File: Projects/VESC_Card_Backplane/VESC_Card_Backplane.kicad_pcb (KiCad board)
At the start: 2 copper layers, 40 parts, among them M1 FE1.1S, P1 USB_OTG, P10 AMP17614426-2_EDGE, P11 CONN_01X06, P2 EC90_Flat, P3 AMP17614426-2_EDGE, P4 CONN_01X06, P5 CONN_01X04, P5V1 CONN_01X02, P6 EC90_Flat, P7 AMP17614426-2_EDGE, P8 CONN_01X06, P9 EC90_Flat, U1 LP38693

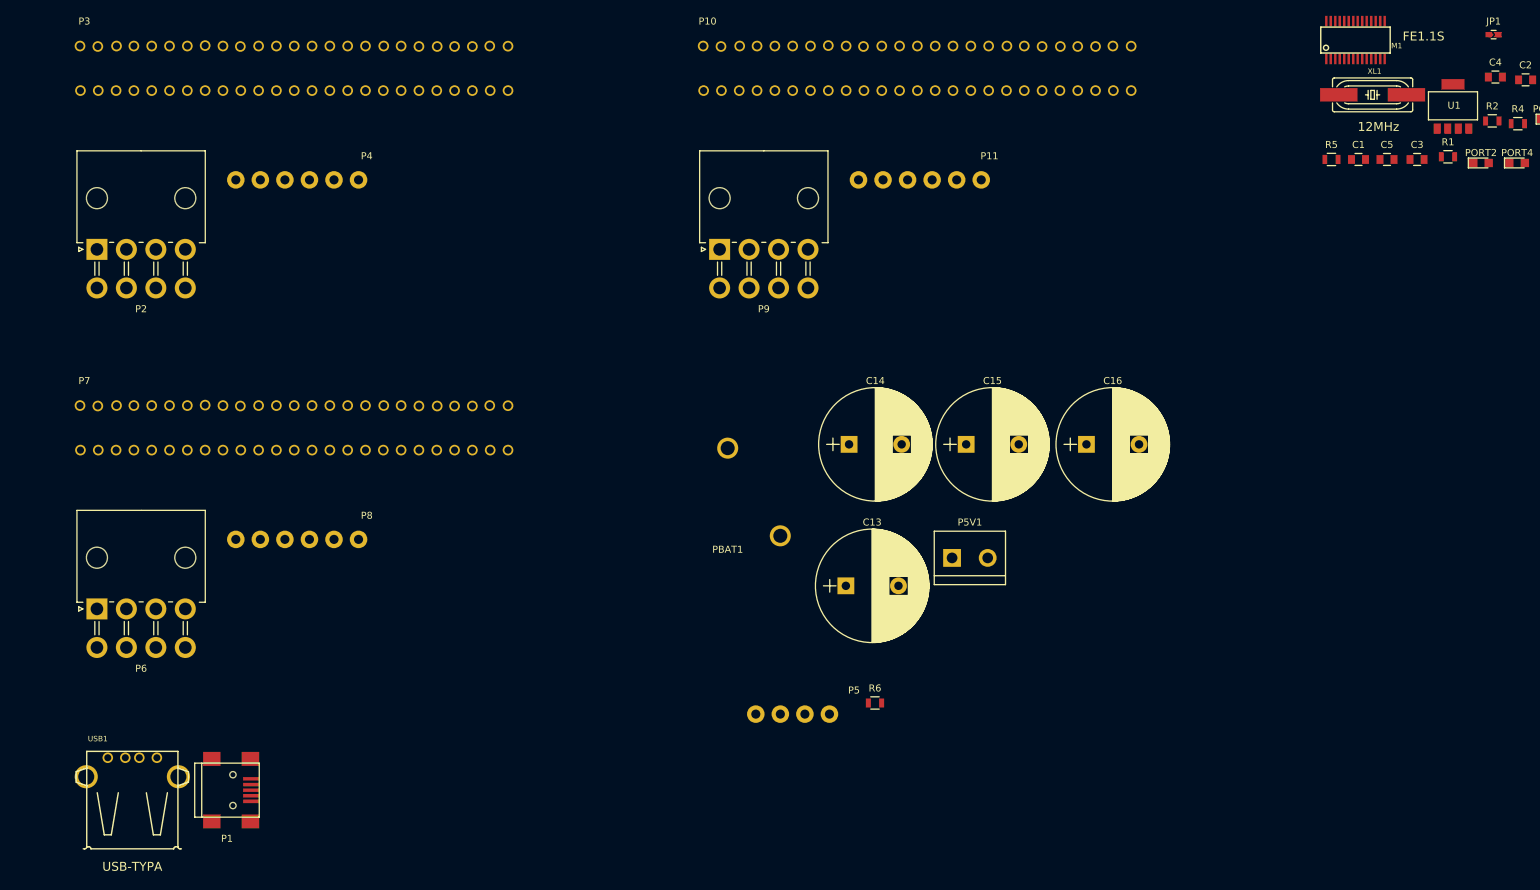
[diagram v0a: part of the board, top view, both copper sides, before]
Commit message: Fixed backplane slot orientation
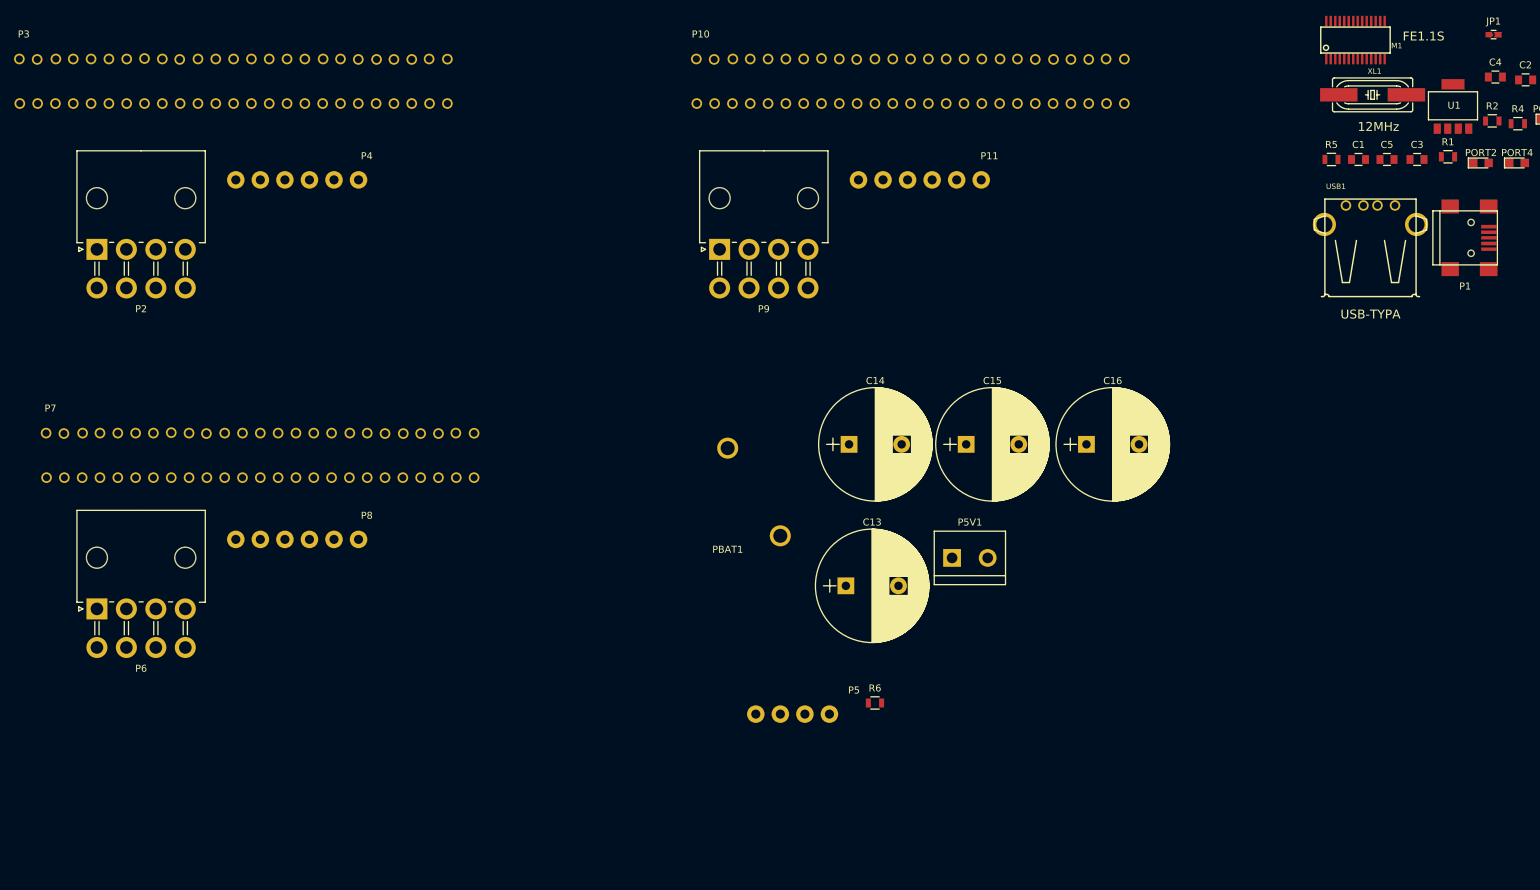
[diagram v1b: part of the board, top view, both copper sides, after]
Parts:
- moved P1 193.3 mm to (241.6, 62.3)
- moved USB1 193.3 mm to (228.1, 63.1)
- moved P3 8.84 mm to (71.1, 50.8)
- moved P7 6.23 mm to (74.9, 104.1)
- moved P10 2.09 mm to (167.6, 50.8)

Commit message: Connected DP's and DM's
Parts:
- ACT1, C1, C2, C3, C4, C5, C6, JP1, PORT1, PORT2, PORT3, PORT4, R1, R2, R3, R4, R5, R6, REXT1, U1: moved to B.Cu
- C14: footprint Capacitors_THT:CP_Radial_D16.0mm_P7.50mm -> Capacitors_ThroughHole:CP_Radial_D8.0mm_P3.80mm
- moved JP1 210.5 mm to (72.9, 153.6), turned to 270 degrees
- moved ACT1 196.0 mm to (82.1, 127.8), turned to 270 degrees
- moved USB1 195.1 mm to (67.6, 173.9)
- moved P1 194.6 mm to (84.2, 176.8), turned to 90 degrees
- moved PORT1 193.0 mm to (82.1, 114.5), turned to 270 degrees
- moved R3 191.4 mm to (91.5, 126.5), turned to 180 degrees
- moved REXT1 189.7 mm to (86.7, 127.9), turned to 180 degrees
- moved XL1 187.1 mm to (83.9, 160.8), turned to 270 degrees
- moved C2 185.4 mm to (84.7, 123.3), turned to 270 degrees
- moved R4 182.7 mm to (81.9, 119.6)
- moved PORT3 182.1 mm to (86.2, 117.2)
- moved M1 181.4 mm to (84.0, 147.1), turned to 180 degrees
- moved C6 177.0 mm to (91.9, 102.9), turned to 90 degrees
- moved PORT4 175.1 mm to (88.6, 121.8), turned to 270 degrees
- moved R2 172.6 mm to (86.7, 113.5)
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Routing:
- net /PGND: track 0.00 -> 167.6 mm
- net +5V: track 0.00 -> 114.8 mm
- net /USB_DP_1: track 0.00 -> 98.2 mm, vias 0 -> 1
- net /USB_DM_1: track 0.00 -> 97.3 mm, vias 0 -> 1
- net /USB_DM_2: track 0.00 -> 66.6 mm
- net /Motor_Controller_A/Y: track 0.00 -> 62.3 mm
- net /USB_DP_2: track 0.00 -> 58.9 mm
- net GND: track 0.00 -> 50.8 mm
- net /Motor_Controller_A/X: track 0.00 -> 50.1 mm
- net /Motor_Controller_A/W: track 0.00 -> 46.1 mm
- net /DM_4: track 0.00 -> 45.5 mm, vias 0 -> 1
- net /DP_4: track 0.00 -> 41.9 mm, vias 0 -> 1
- net /USB_Hub/DM_U: track 0.00 -> 27.1 mm
- net /USB_Hub/DP_U: track 0.00 -> 26.6 mm
- net Net-(P1-Pad5): track 0.00 -> 13.9 mm
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
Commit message: Comleted VESC Backplane
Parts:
- removed JP1: Jumper_NC_Small, USST-footprints:J_0603
- removed U1: LP38693, USST-footprints:SOT-223_5-pin
- added JP2: J, USST-footprints:J_0603, F.Cu at (86.0, 132.4)
- added P12: CONN_01X02, Pin_Headers:Pin_Header_Straight_2x01_Pitch1.27mm, F.Cu at (30.2, 36.6)
- added P13: CONN_01X02, Pin_Headers:Pin_Header_Straight_2x01_Pitch1.27mm, F.Cu at (30.2, 68.1)
- added P14: CONN_01X02, Pin_Headers:Pin_Header_Straight_2x01_Pitch1.27mm, F.Cu at (30.2, 99.6)
- ACT1, C1, C2, C3, C4, C5, C6, PORT1, PORT2, PORT3, PORT4, R1, R2, R3, R4, R5, R6, REXT1: moved to F.Cu
- P11, P4, P8: footprint USST-footprints:Molex_39502_1006R -> Pin_Headers:Pin_Header_Angled_2x03_Pitch2.54mm
- P2, P6, P9: footprint Connectors_Molex:Molex_MiniFit-JR-5569-08A2_2x04x4.20mm_Angled -> USST-footprints:Molex_MiniFit-JR-5569-08A2_2x04x4.20mm_Angled_Overhang
- moved P11 62.4 mm to (35.0, 107.6), turned to 180 degrees
- moved P8 60.0 mm to (35.0, 76.2), turned to 180 degrees
- moved P4 59.8 mm to (35.0, 44.6), turned to 180 degrees
- moved P5 50.6 mm to (49.0, 137.5), turned to 0 degrees
- moved R6 49.7 mm to (54.2, 132.1)
- moved P10 48.2 mm to (80.2, 99.0)
- moved P5V1 44.7 mm to (37.5, 135.0), turned to 270 degrees
- moved XL1 40.8 mm to (102.5, 124.5), turned to 90 degrees
- moved P1 37.7 mm to (92.5, 140.0)
- moved USB1 34.7 mm to (75.0, 140.0)
- moved P7 33.2 mm to (80.4, 68.9)
- moved C1 29.6 mm to (98.5, 127.4)
- moved PBAT1 29.5 mm to (37.5, 122.5), turned to 90 degrees
- moved C14 29.1 mm to (66.2, 125.0)
- moved ACT1 26.7 mm to (104.5, 113.2), turned to 0 degrees
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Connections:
- M1 pad 25: Net-(M1-Pad25) -> (no net)
- M1 pad 27: Net-(M1-Pad27) -> (no net)
- M1 pad 8: /USB_DP_2 -> /USB_DM_2
- M1 pad 9: /USB_DM_2 -> /USB_DP_2
- P1 pad 1: +5V -> Net-(JP2-Pad2)
- P1 pad 4: Net-(P1-Pad4) -> (no net)
- P1 pad 5: Net-(P1-Pad5) -> GND
- P1 pad 6: Net-(P1-Pad5) -> GND
- P10 pad 21: Net-(P10-Pad21) -> /Motor_Controller_C/GND_AUX
- P11 pad 1: Net-(P10-Pad21) -> Net-(P10-Pad17)
- P11 pad 2: Net-(P10-Pad20) -> Net-(P10-Pad16)
- P11 pad 5: Net-(P10-Pad17) -> Net-(P10-Pad20)
- P11 pad 6: Net-(P10-Pad16) -> /Motor_Controller_C/GND_AUX
- P3 pad 21: Net-(P3-Pad21) -> /Motor_Controller_A/GND_AUX
- P3 pad 24: GND -> /PGND
- P3 pad 25: GND -> /PGND
- P4 pad 1: Net-(P3-Pad21) -> Net-(P3-Pad17)
- P4 pad 2: Net-(P3-Pad20) -> Net-(P3-Pad16)
- P4 pad 5: Net-(P3-Pad17) -> Net-(P3-Pad20)
- P4 pad 6: Net-(P3-Pad16) -> /Motor_Controller_A/GND_AUX
- P7 pad 21: Net-(P7-Pad21) -> /Motor_Controller_B/GND_AUX
- P7 pad 24: GND -> /PGND
- P7 pad 25: GND -> /PGND
- P8 pad 1: Net-(P7-Pad21) -> Net-(P7-Pad17)
- P8 pad 2: Net-(P7-Pad20) -> Net-(P7-Pad16)
- P8 pad 5: Net-(P7-Pad17) -> Net-(P7-Pad20)
- P8 pad 6: Net-(P7-Pad16) -> /Motor_Controller_B/GND_AUX
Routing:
- net /CANH: track 0.00 -> 262.0 mm
- net /CAN_Bus/CANL: track 0.00 -> 247.3 mm, vias 0 -> 4
- net +5V: track 114.8 -> 346.6 mm, vias 0 -> 2
- net GND: track 50.8 -> 219.2 mm, vias 0 -> 2
- net /Motor_Controller_B/Y: track 0.00 -> 120.6 mm
- net /Motor_Controller_C/Y: track 0.00 -> 116.1 mm
- net /VBAT: track 0.00 -> 110.0 mm
- net /Motor_Controller_B/X: track 0.00 -> 86.6 mm
- net /Motor_Controller_C/X: track 0.00 -> 84.8 mm
- net Net-(P12-Pad2): track 0.00 -> 84.2 mm
- net Net-(P10-Pad15): track 0.00 -> 84.0 mm
- net Net-(P7-Pad16): track 0.00 -> 83.3 mm
- net Net-(P10-Pad16): track 0.00 -> 83.2 mm
- net Net-(P3-Pad16): track 0.00 -> 83.1 mm
- net Net-(P13-Pad2): track 0.00 -> 82.3 mm
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- added copper zone on B.Cu, net /PGND
- added copper zone on F.Cu, net /PGND
- added copper zone on B.Cu, net /VBAT
- added copper zone on F.Cu, net /VBAT
- added copper zone on B.Cu, net GND
- added copper zone on F.Cu, net GND
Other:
- board outline added: 82 x 131 mm
- net class Default: trace_width 0.25 -> 0.2032; via_dia 0.6 -> 0.508; via_drill 0.4 -> 0.254
- rule trace_min: 0.2 -> 0.2032
- rule via_min_drill: 0.3 -> 0.254
- rule via_min_size: 0.4 -> 0.508

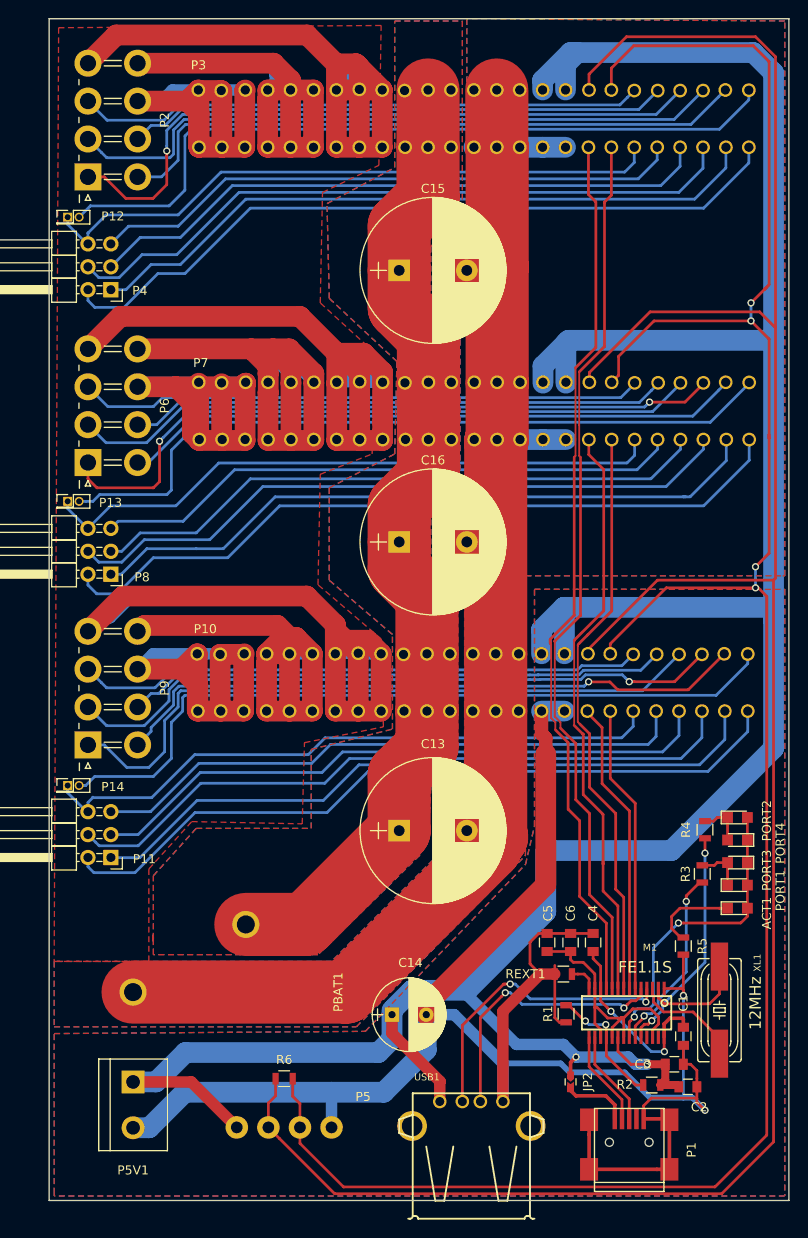
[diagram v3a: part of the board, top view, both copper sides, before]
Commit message: Added VESC Breakout project
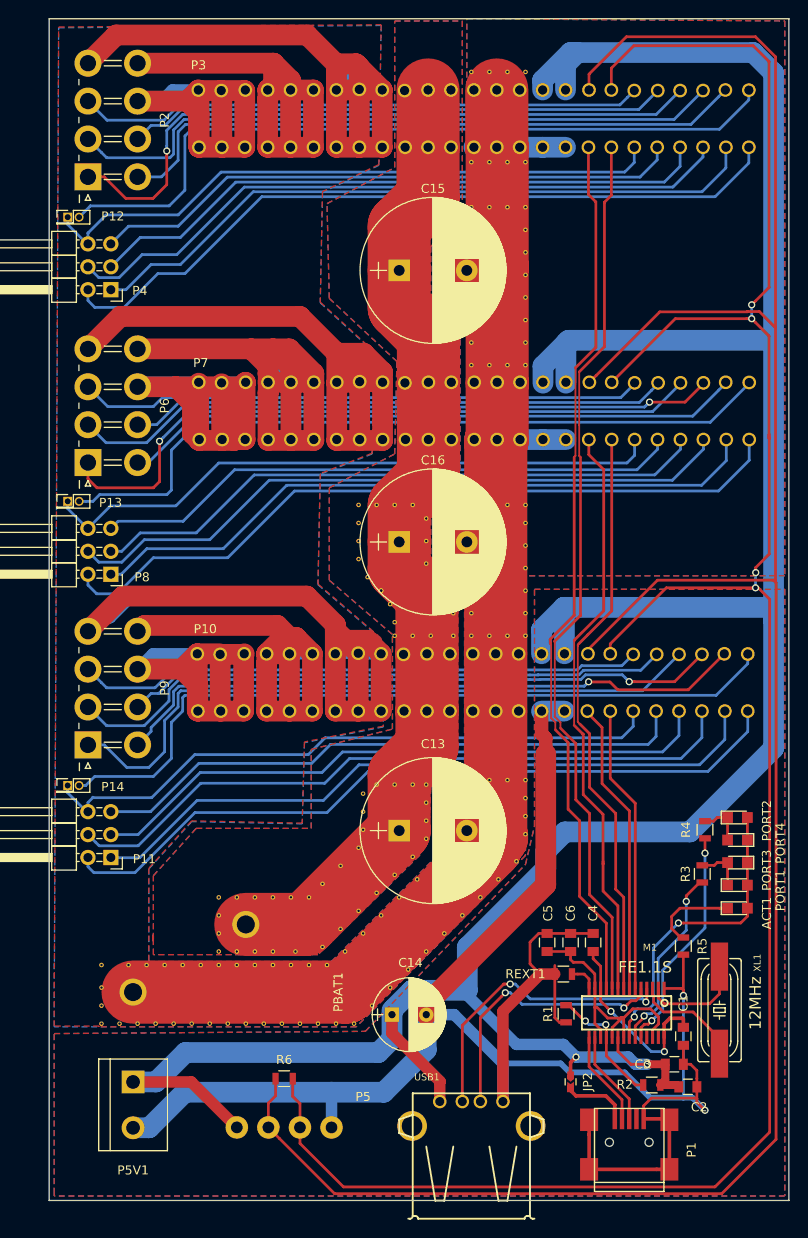
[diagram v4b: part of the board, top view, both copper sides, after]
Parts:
- added REF**: VIA_STICH_0.5, USST-footprints:VIA_STICH_0.5, F.Cu at (70.5, 83.0)
- added REF**: VIA_STICH_0.5, USST-footprints:VIA_STICH_0.5, F.Cu at (62.5, 72.5)
- added REF**: VIA_STICH_0.5, USST-footprints:VIA_STICH_0.5, F.Cu at (81.0, 80.5)
- added REF**: VIA_STICH_0.5, USST-footprints:VIA_STICH_0.5, F.Cu at (75.0, 83.0)
- added REF**: VIA_STICH_0.5, USST-footprints:VIA_STICH_0.5, F.Cu at (77.0, 83.0)
- added REF**: VIA_STICH_0.5, USST-footprints:VIA_STICH_0.5, F.Cu at (79.0, 83.0)
- added REF**: VIA_STICH_0.5, USST-footprints:VIA_STICH_0.5, F.Cu at (81.0, 83.0)
- added REF**: VIA_STICH_0.5, USST-footprints:VIA_STICH_0.5, F.Cu at (34.0, 119.5)
- added REF**: VIA_STICH_0.5, USST-footprints:VIA_STICH_0.5, F.Cu at (37.0, 119.5)
- added REF**: VIA_STICH_0.5, USST-footprints:VIA_STICH_0.5, F.Cu at (39.0, 119.5)
- added REF**: VIA_STICH_0.5, USST-footprints:VIA_STICH_0.5, F.Cu at (41.0, 119.5)
- added REF**: VIA_STICH_0.5, USST-footprints:VIA_STICH_0.5, F.Cu at (43.0, 119.5)
- added REF**: VIA_STICH_0.5, USST-footprints:VIA_STICH_0.5, F.Cu at (62.5, 70.5)
- added REF**: VIA_STICH_0.5, USST-footprints:VIA_STICH_0.5, F.Cu at (45.0, 119.5)
- added REF**: VIA_STICH_0.5, USST-footprints:VIA_STICH_0.5, F.Cu at (47.0, 119.5)
- added REF**: VIA_STICH_0.5, USST-footprints:VIA_STICH_0.5, F.Cu at (49.0, 119.5)
- added REF**: VIA_STICH_0.5, USST-footprints:VIA_STICH_0.5, F.Cu at (51.0, 119.5)
- added REF**: VIA_STICH_0.5, USST-footprints:VIA_STICH_0.5, F.Cu at (53.0, 119.5)
- added REF**: VIA_STICH_0.5, USST-footprints:VIA_STICH_0.5, F.Cu at (55.0, 119.5)
- added REF**: VIA_STICH_0.5, USST-footprints:VIA_STICH_0.5, F.Cu at (57.0, 119.5)
- added REF**: VIA_STICH_0.5, USST-footprints:VIA_STICH_0.5, F.Cu at (59.0, 119.5)
- added REF**: VIA_STICH_0.5, USST-footprints:VIA_STICH_0.5, F.Cu at (61.0, 118.0)
- added REF**: VIA_STICH_0.5, USST-footprints:VIA_STICH_0.5, F.Cu at (63.0, 116.0)
- added REF**: VIA_STICH_0.5, USST-footprints:VIA_STICH_0.5, F.Cu at (62.5, 68.5)
- added REF**: VIA_STICH_0.5, USST-footprints:VIA_STICH_0.5, F.Cu at (65.0, 114.0)
- added REF**: VIA_STICH_0.5, USST-footprints:VIA_STICH_0.5, F.Cu at (67.0, 112.0)
- added REF**: VIA_STICH_0.5, USST-footprints:VIA_STICH_0.5, F.Cu at (69.0, 110.0)
- added REF**: VIA_STICH_0.5, USST-footprints:VIA_STICH_0.5, F.Cu at (71.0, 108.0)
- added REF**: VIA_STICH_0.5, USST-footprints:VIA_STICH_0.5, F.Cu at (72.0, 106.0)
- added REF**: VIA_STICH_0.5, USST-footprints:VIA_STICH_0.5, F.Cu at (72.0, 104.0)
- added REF**: VIA_STICH_0.5, USST-footprints:VIA_STICH_0.5, F.Cu at (73.0, 102.5)
- added REF**: VIA_STICH_0.5, USST-footprints:VIA_STICH_0.5, F.Cu at (74.0, 101.0)
- added REF**: VIA_STICH_0.5, USST-footprints:VIA_STICH_0.5, F.Cu at (75.0, 99.0)
- added REF**: VIA_STICH_0.5, USST-footprints:VIA_STICH_0.5, F.Cu at (77.0, 99.0)
- added REF**: VIA_STICH_0.5, USST-footprints:VIA_STICH_0.5, F.Cu at (64.5, 68.5)
- added REF**: VIA_STICH_0.5, USST-footprints:VIA_STICH_0.5, F.Cu at (79.0, 99.0)
- added REF**: VIA_STICH_0.5, USST-footprints:VIA_STICH_0.5, F.Cu at (81.0, 99.0)
- added REF**: VIA_STICH_0.5, USST-footprints:VIA_STICH_0.5, F.Cu at (81.0, 101.0)
- added REF**: VIA_STICH_0.5, USST-footprints:VIA_STICH_0.5, F.Cu at (81.0, 103.0)
- added REF**: VIA_STICH_0.5, USST-footprints:VIA_STICH_0.5, F.Cu at (81.0, 105.0)
- added REF**: VIA_STICH_0.5, USST-footprints:VIA_STICH_0.5, F.Cu at (80.0, 108.0)
- added REF**: VIA_STICH_0.5, USST-footprints:VIA_STICH_0.5, F.Cu at (78.0, 110.0)
- added REF**: VIA_STICH_0.5, USST-footprints:VIA_STICH_0.5, F.Cu at (76.0, 112.0)
- added REF**: VIA_STICH_0.5, USST-footprints:VIA_STICH_0.5, F.Cu at (74.0, 114.0)
- added REF**: VIA_STICH_0.5, USST-footprints:VIA_STICH_0.5, F.Cu at (72.0, 116.0)
- added REF**: VIA_STICH_0.5, USST-footprints:VIA_STICH_0.5, F.Cu at (66.5, 68.5)
- added REF**: VIA_STICH_0.5, USST-footprints:VIA_STICH_0.5, F.Cu at (70.0, 118.0)
- added REF**: VIA_STICH_0.5, USST-footprints:VIA_STICH_0.5, F.Cu at (68.0, 120.0)
- added REF**: VIA_STICH_0.5, USST-footprints:VIA_STICH_0.5, F.Cu at (66.0, 122.0)
- added REF**: VIA_STICH_0.5, USST-footprints:VIA_STICH_0.5, F.Cu at (64.0, 124.0)
- added REF**: VIA_STICH_0.5, USST-footprints:VIA_STICH_0.5, F.Cu at (62.0, 126.0)
- added REF**: VIA_STICH_0.5, USST-footprints:VIA_STICH_0.5, F.Cu at (60.0, 126.0)
- added REF**: VIA_STICH_0.5, USST-footprints:VIA_STICH_0.5, F.Cu at (58.0, 126.0)
- added REF**: VIA_STICH_0.5, USST-footprints:VIA_STICH_0.5, F.Cu at (56.0, 126.0)
- added REF**: VIA_STICH_0.5, USST-footprints:VIA_STICH_0.5, F.Cu at (54.0, 126.0)
- added REF**: VIA_STICH_0.5, USST-footprints:VIA_STICH_0.5, F.Cu at (52.0, 126.0)
- added REF**: VIA_STICH_0.5, USST-footprints:VIA_STICH_0.5, F.Cu at (68.5, 68.5)
- added REF**: VIA_STICH_0.5, USST-footprints:VIA_STICH_0.5, F.Cu at (50.0, 126.0)
- added REF**: VIA_STICH_0.5, USST-footprints:VIA_STICH_0.5, F.Cu at (48.0, 126.0)
- added REF**: VIA_STICH_0.5, USST-footprints:VIA_STICH_0.5, F.Cu at (46.0, 126.0)
- added REF**: VIA_STICH_0.5, USST-footprints:VIA_STICH_0.5, F.Cu at (44.0, 126.0)
- added REF**: VIA_STICH_0.5, USST-footprints:VIA_STICH_0.5, F.Cu at (34.0, 122.0)
- added REF**: VIA_STICH_0.5, USST-footprints:VIA_STICH_0.5, F.Cu at (34.0, 124.0)
- added REF**: VIA_STICH_0.5, USST-footprints:VIA_STICH_0.5, F.Cu at (34.0, 126.0)
- added REF**: VIA_STICH_0.5, USST-footprints:VIA_STICH_0.5, F.Cu at (36.0, 126.0)
- added REF**: VIA_STICH_0.5, USST-footprints:VIA_STICH_0.5, F.Cu at (38.0, 126.0)
- added REF**: VIA_STICH_0.5, USST-footprints:VIA_STICH_0.5, F.Cu at (40.0, 126.0)
- added REF**: VIA_STICH_0.5, USST-footprints:VIA_STICH_0.5, F.Cu at (71.0, 68.5)
- added REF**: VIA_STICH_0.5, USST-footprints:VIA_STICH_0.5, F.Cu at (42.0, 126.0)
- added REF**: VIA_STICH_0.5, USST-footprints:VIA_STICH_0.5, F.Cu at (70.0, 70.0)
- added REF**: VIA_STICH_0.5, USST-footprints:VIA_STICH_0.5, F.Cu at (70.0, 72.5)
- added REF**: VIA_STICH_0.5, USST-footprints:VIA_STICH_0.5, F.Cu at (70.0, 75.0)
- added REF**: VIA_STICH_0.5, USST-footprints:VIA_STICH_0.5, F.Cu at (68.5, 83.0)
- added REF**: VIA_STICH_0.5, USST-footprints:VIA_STICH_0.5, F.Cu at (71.0, 77.0)
- added REF**: VIA_STICH_0.5, USST-footprints:VIA_STICH_0.5, F.Cu at (72.5, 78.5)
- added REF**: VIA_STICH_0.5, USST-footprints:VIA_STICH_0.5, F.Cu at (73.0, 80.5)
- added REF**: VIA_STICH_0.5, USST-footprints:VIA_STICH_0.5, F.Cu at (73.0, 83.0)
- added REF**: VIA_STICH_0.5, USST-footprints:VIA_STICH_0.5, F.Cu at (63.0, 100.5)
- added REF**: VIA_STICH_0.5, USST-footprints:VIA_STICH_0.5, F.Cu at (63.0, 102.5)
- added REF**: VIA_STICH_0.5, USST-footprints:VIA_STICH_0.5, F.Cu at (63.0, 104.5)
- added REF**: VIA_STICH_0.5, USST-footprints:VIA_STICH_0.5, F.Cu at (49.0, 118.0)
- added REF**: VIA_STICH_0.5, USST-footprints:VIA_STICH_0.5, F.Cu at (51.0, 118.0)
- added REF**: VIA_STICH_0.5, USST-footprints:VIA_STICH_0.5, F.Cu at (53.0, 118.0)
- added REF**: VIA_STICH_0.5, USST-footprints:VIA_STICH_0.5, F.Cu at (66.5, 83.0)
- added REF**: VIA_STICH_0.5, USST-footprints:VIA_STICH_0.5, F.Cu at (55.5, 118.0)
- added REF**: VIA_STICH_0.5, USST-footprints:VIA_STICH_0.5, F.Cu at (58.5, 117.5)
- added REF**: VIA_STICH_0.5, USST-footprints:VIA_STICH_0.5, F.Cu at (60.5, 115.5)
- added REF**: VIA_STICH_0.5, USST-footprints:VIA_STICH_0.5, F.Cu at (62.5, 113.5)
- added REF**: VIA_STICH_0.5, USST-footprints:VIA_STICH_0.5, F.Cu at (64.5, 111.5)
- added REF**: VIA_STICH_0.5, USST-footprints:VIA_STICH_0.5, F.Cu at (66.5, 109.5)
- added REF**: VIA_STICH_0.5, USST-footprints:VIA_STICH_0.5, F.Cu at (68.5, 107.5)
- added REF**: VIA_STICH_0.5, USST-footprints:VIA_STICH_0.5, F.Cu at (70.0, 105.5)
- added REF**: VIA_STICH_0.5, USST-footprints:VIA_STICH_0.5, F.Cu at (70.0, 103.5)
- added REF**: VIA_STICH_0.5, USST-footprints:VIA_STICH_0.5, F.Cu at (70.0, 101.5)
- added REF**: VIA_STICH_0.5, USST-footprints:VIA_STICH_0.5, F.Cu at (66.5, 81.5)
- added REF**: VIA_STICH_0.5, USST-footprints:VIA_STICH_0.5, F.Cu at (70.0, 99.5)
- added REF**: VIA_STICH_0.5, USST-footprints:VIA_STICH_0.5, F.Cu at (68.5, 99.5)
- added REF**: VIA_STICH_0.5, USST-footprints:VIA_STICH_0.5, F.Cu at (66.5, 99.5)
- added REF**: VIA_STICH_0.5, USST-footprints:VIA_STICH_0.5, F.Cu at (64.5, 99.5)
- added REF**: VIA_STICH_0.5, USST-footprints:VIA_STICH_0.5, F.Cu at (62.5, 106.5)
- added REF**: VIA_STICH_0.5, USST-footprints:VIA_STICH_0.5, F.Cu at (60.5, 108.5)
- added REF**: VIA_STICH_0.5, USST-footprints:VIA_STICH_0.5, F.Cu at (58.5, 110.5)
- added REF**: VIA_STICH_0.5, USST-footprints:VIA_STICH_0.5, F.Cu at (57.0, 112.0)
- added REF**: VIA_STICH_0.5, USST-footprints:VIA_STICH_0.5, F.Cu at (55.0, 112.0)
- added REF**: VIA_STICH_0.5, USST-footprints:VIA_STICH_0.5, F.Cu at (53.0, 112.0)
- added REF**: VIA_STICH_0.5, USST-footprints:VIA_STICH_0.5, F.Cu at (66.0, 79.5)
- added REF**: VIA_STICH_0.5, USST-footprints:VIA_STICH_0.5, F.Cu at (51.0, 112.0)
- added REF**: VIA_STICH_0.5, USST-footprints:VIA_STICH_0.5, F.Cu at (49.0, 112.0)
- added REF**: VIA_STICH_0.5, USST-footprints:VIA_STICH_0.5, F.Cu at (47.0, 112.0)
- added REF**: VIA_STICH_0.5, USST-footprints:VIA_STICH_0.5, F.Cu at (47.0, 114.0)
- added REF**: VIA_STICH_0.5, USST-footprints:VIA_STICH_0.5, F.Cu at (47.0, 116.0)
- added REF**: VIA_STICH_0.5, USST-footprints:VIA_STICH_0.5, F.Cu at (47.0, 118.0)
- added REF**: VIA_STICH_0.5, USST-footprints:VIA_STICH_0.5, F.Cu at (75.0, 20.5)
- added REF**: VIA_STICH_0.5, USST-footprints:VIA_STICH_0.5, F.Cu at (77.0, 20.5)
- added REF**: VIA_STICH_0.5, USST-footprints:VIA_STICH_0.5, F.Cu at (79.0, 20.5)
- added REF**: VIA_STICH_0.5, USST-footprints:VIA_STICH_0.5, F.Cu at (81.0, 20.5)
- added REF** (x2): VIA_STICH_0.5, USST-footprints:VIA_STICH_0.5, F.Cu at (65.0, 78.0)
- added REF**: VIA_STICH_0.5, USST-footprints:VIA_STICH_0.5, F.Cu at (81.0, 30.5)
- added REF**: VIA_STICH_0.5, USST-footprints:VIA_STICH_0.5, F.Cu at (79.0, 30.5)
- added REF**: VIA_STICH_0.5, USST-footprints:VIA_STICH_0.5, F.Cu at (77.0, 30.5)
- added REF**: VIA_STICH_0.5, USST-footprints:VIA_STICH_0.5, F.Cu at (75.0, 30.5)
- added REF**: VIA_STICH_0.5, USST-footprints:VIA_STICH_0.5, F.Cu at (75.0, 46.0)
- added REF**: VIA_STICH_0.5, USST-footprints:VIA_STICH_0.5, F.Cu at (73.5, 45.0)
- added REF**: VIA_STICH_0.5, USST-footprints:VIA_STICH_0.5, F.Cu at (72.0, 43.5)
- added REF**: VIA_STICH_0.5, USST-footprints:VIA_STICH_0.5, F.Cu at (72.0, 41.5)
- added REF**: VIA_STICH_0.5, USST-footprints:VIA_STICH_0.5, F.Cu at (73.0, 39.5)
- added REF**: VIA_STICH_0.5, USST-footprints:VIA_STICH_0.5, F.Cu at (75.0, 38.0)
- added REF**: VIA_STICH_0.5, USST-footprints:VIA_STICH_0.5, F.Cu at (75.0, 35.5)
- added REF**: VIA_STICH_0.5, USST-footprints:VIA_STICH_0.5, F.Cu at (77.0, 35.5)
- added REF**: VIA_STICH_0.5, USST-footprints:VIA_STICH_0.5, F.Cu at (79.0, 35.5)
- added REF**: VIA_STICH_0.5, USST-footprints:VIA_STICH_0.5, F.Cu at (81.0, 35.5)
- added REF**: VIA_STICH_0.5, USST-footprints:VIA_STICH_0.5, F.Cu at (81.0, 38.0)
- added REF**: VIA_STICH_0.5, USST-footprints:VIA_STICH_0.5, F.Cu at (81.0, 40.5)
- added REF**: VIA_STICH_0.5, USST-footprints:VIA_STICH_0.5, F.Cu at (81.0, 43.0)
- added REF**: VIA_STICH_0.5, USST-footprints:VIA_STICH_0.5, F.Cu at (81.0, 45.5)
- added REF**: VIA_STICH_0.5, USST-footprints:VIA_STICH_0.5, F.Cu at (81.0, 48.0)
- added REF**: VIA_STICH_0.5, USST-footprints:VIA_STICH_0.5, F.Cu at (81.0, 50.5)
- added REF**: VIA_STICH_0.5, USST-footprints:VIA_STICH_0.5, F.Cu at (63.5, 76.5)
- added REF**: VIA_STICH_0.5, USST-footprints:VIA_STICH_0.5, F.Cu at (75.0, 48.0)
- added REF**: VIA_STICH_0.5, USST-footprints:VIA_STICH_0.5, F.Cu at (75.0, 50.5)
- added REF**: VIA_STICH_0.5, USST-footprints:VIA_STICH_0.5, F.Cu at (75.0, 53.0)
- added REF**: VIA_STICH_0.5, USST-footprints:VIA_STICH_0.5, F.Cu at (77.0, 53.0)
- added REF**: VIA_STICH_0.5, USST-footprints:VIA_STICH_0.5, F.Cu at (79.0, 53.0)
- added REF**: VIA_STICH_0.5, USST-footprints:VIA_STICH_0.5, F.Cu at (81.0, 53.0)
- added REF**: VIA_STICH_0.5, USST-footprints:VIA_STICH_0.5, F.Cu at (75.0, 80.5)
- added REF**: VIA_STICH_0.5, USST-footprints:VIA_STICH_0.5, F.Cu at (75.0, 78.0)
- added REF**: VIA_STICH_0.5, USST-footprints:VIA_STICH_0.5, F.Cu at (74.0, 75.5)
- added REF**: VIA_STICH_0.5, USST-footprints:VIA_STICH_0.5, F.Cu at (72.5, 73.5)
- added REF**: VIA_STICH_0.5, USST-footprints:VIA_STICH_0.5, F.Cu at (62.5, 74.5)
- added REF**: VIA_STICH_0.5, USST-footprints:VIA_STICH_0.5, F.Cu at (72.5, 71.5)
- added REF**: VIA_STICH_0.5, USST-footprints:VIA_STICH_0.5, F.Cu at (73.5, 70.0)
- added REF**: VIA_STICH_0.5, USST-footprints:VIA_STICH_0.5, F.Cu at (75.0, 68.5)
- added REF**: VIA_STICH_0.5, USST-footprints:VIA_STICH_0.5, F.Cu at (77.0, 68.5)
- added REF**: VIA_STICH_0.5, USST-footprints:VIA_STICH_0.5, F.Cu at (79.0, 68.5)
- added REF**: VIA_STICH_0.5, USST-footprints:VIA_STICH_0.5, F.Cu at (81.0, 68.5)
- added REF**: VIA_STICH_0.5, USST-footprints:VIA_STICH_0.5, F.Cu at (81.0, 70.5)
- added REF**: VIA_STICH_0.5, USST-footprints:VIA_STICH_0.5, F.Cu at (81.0, 73.0)
- added REF**: VIA_STICH_0.5, USST-footprints:VIA_STICH_0.5, F.Cu at (81.0, 75.5)
- added REF**: VIA_STICH_0.5, USST-footprints:VIA_STICH_0.5, F.Cu at (81.0, 78.0)
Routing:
- net /Motor_Controller_B/W: track 55.6 -> 61.9 mm
- net /Motor_Controller_C/W: track 52.0 -> 57.2 mm
- net /Motor_Controller_B/X: track 86.6 -> 91.7 mm
- net /Motor_Controller_A/X: track 81.3 -> 84.6 mm
- net /Motor_Controller_A/W: track 52.0 -> 54.6 mm
- net /CAN_Bus/CANL: track 247.3 -> 246.1 mm
- net Net-(P3-Pad18): track 76.0 -> 75.3 mm
